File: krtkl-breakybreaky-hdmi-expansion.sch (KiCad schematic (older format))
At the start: 39 parts, among them J1 SMH-120-02-T-D, J2 685119134923, J3 solder_jumper, Q1 BSS138AKA, Q2 BSS138AKA, Q3 BSS138AKA, U1 TPD12S016PWR, U2 TPS61232DRCT

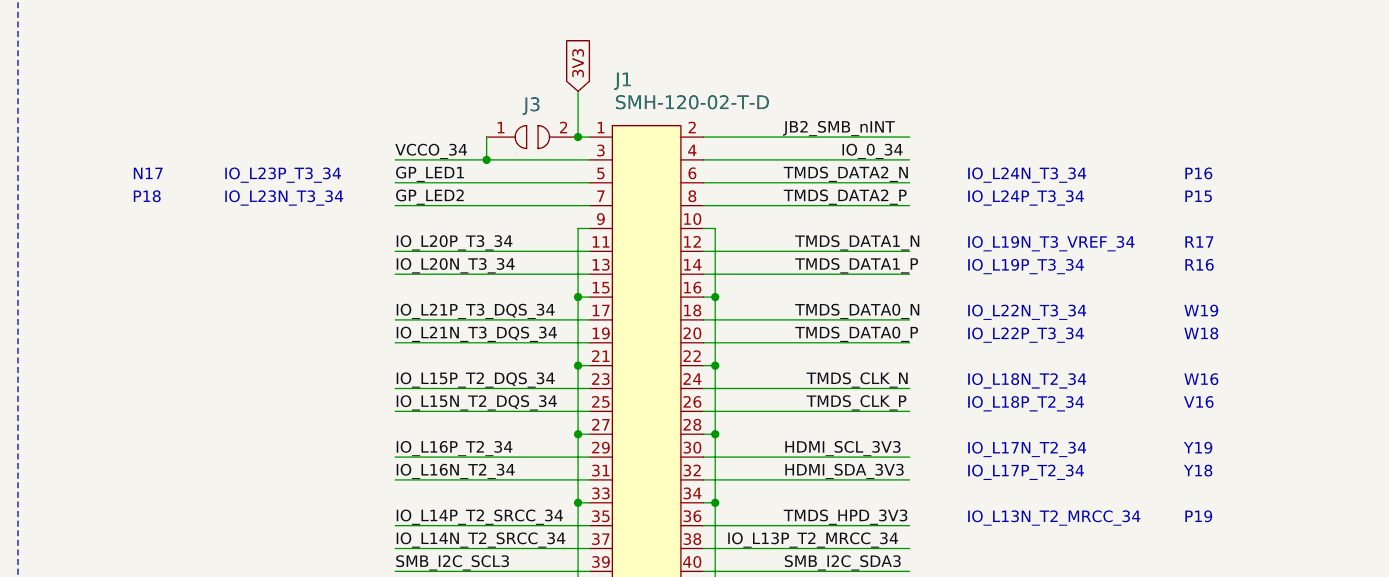
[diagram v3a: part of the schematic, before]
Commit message: Changed CLK connection on 40-pin connector
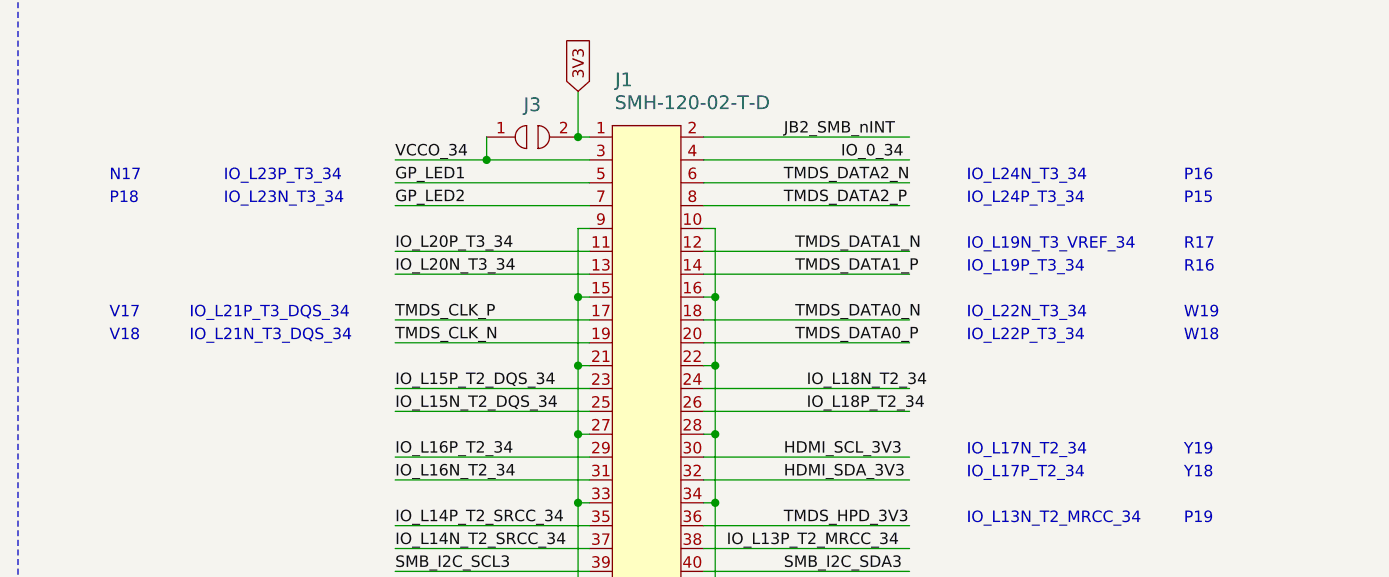
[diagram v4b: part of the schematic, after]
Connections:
- net labels added: IO_L18N_T2_34, IO_L18P_T2_34
- net labels removed: IO_L21N_T3_DQS_34, IO_L21P_T3_DQS_34
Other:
- note added: "IO_L21N_T3_DQS_34"
- note added: "IO_L21P_T3_DQS_34"
- note added: "V17"
- note added: "V18"
- note removed: "IO_L18N_T2_34"
- note removed: "IO_L18P_T2_34"
- note removed: "V16"
- note removed: "W16"
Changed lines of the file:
@@
 Text Label 2650 6800 0    50   ~ 0
 IO_L20N_T3_34
-Text Label 2650 7000 0    50   ~ 0
-IO_L21P_T3_DQS_34
-Text Label 2650 7100 0    50   ~ 0
-IO_L21N_T3_DQS_34
 Text Label 2650 7300 0    50   ~ 0
 IO_L15P_T2_DQS_34
@@
 TMDS_DATA1_N
 Text Label 4450 7400 0    50   ~ 0
-TMDS_CLK_P
+IO_L18P_T2_34
 Text Label 4450 7300 0    50   ~ 0
-TMDS_CLK_N
+IO_L18N_T2_34
 Text Label 4350 7600 0    50   ~ 0
 HDMI_SCL_3V3
@@
 Text Notes 5150 7100 0    50   ~ 0
 IO_L22P_T3_34
-Text Notes 5150 7300 0    50   ~ 0
-IO_L18N_T2_34
-Text Notes 5150 7400 0    50   ~ 0
-IO_L18P_T2_34
 Text Notes 5150 7600 0    50   ~ 0
 IO_L17N_T2_34
@@
 Text Notes 6100 7100 0    50   ~ 0
 W18
-Text Notes 6100 7300 0    50   ~ 0
-W16
-Text Notes 6100 7400 0    50   ~ 0
-V16
 Text Notes 6100 7600 0    50   ~ 0
 Y19
@@
 Text Notes 6100 7900 0    50   ~ 0
 P19
-Text Notes 1500 6500 0    50   ~ 0
+Text Notes 1400 6500 0    50   ~ 0
 P18
-Text Notes 1500 6400 0    50   ~ 0
+Text Notes 1400 6400 0    50   ~ 0
 N17
 $Comp
@@
 Wire Wire Line
 	8650 6550 8650 6600
+Text Label 2650 7100 0    50   ~ 0
+TMDS_CLK_N
+Text Label 2650 7000 0    50   ~ 0
+TMDS_CLK_P
+Text Notes 1750 7000 0    50   ~ 0
+IO_L21P_T3_DQS_34
+Text Notes 1750 7100 0    50   ~ 0
+IO_L21N_T3_DQS_34
+Text Notes 1400 7000 0    50   ~ 0
+V17
+Text Notes 1400 7100 0    50   ~ 0
+V18
 $EndSCHEMATC
